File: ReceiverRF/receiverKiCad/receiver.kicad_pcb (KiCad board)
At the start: 2 copper layers, 95 x 60 mm, 75 parts, among them J1 Conn_Coaxial, J2 Conn_01x05_Socket, J3 Conn_01x04, Q1 MMBT3904, SW1 SW_Push, SW2 SW_Push, SW3 SW_Push, SW4 SW_Push, SW5 SW_Nidec_CAS-120A1, U1 STM32F103RET6, U2 NCV5501DT33RKG, U3 NJM2882F05-TE1, U4 MLX90393SLW-ABA-011-RE, Y1 Crystal_GND24

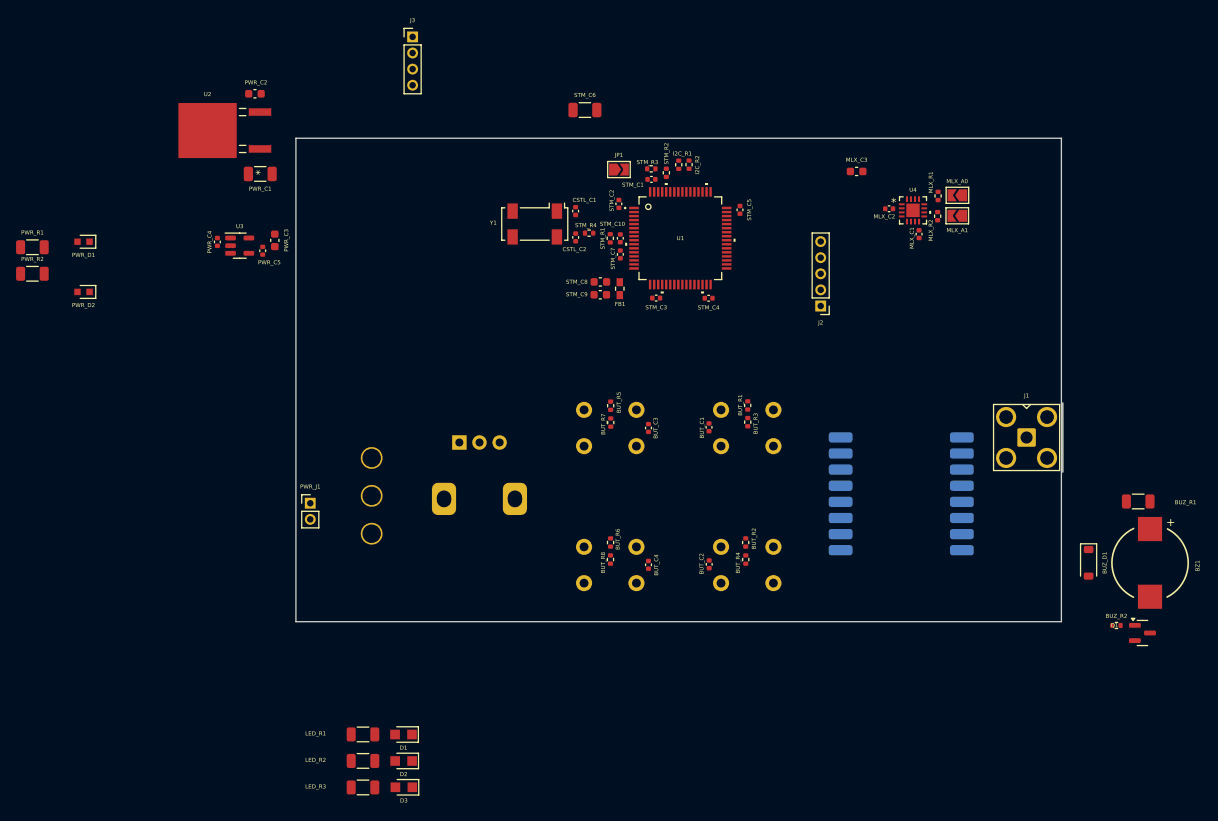
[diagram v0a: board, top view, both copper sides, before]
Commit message: suggestions de Luca et placement sur PCB
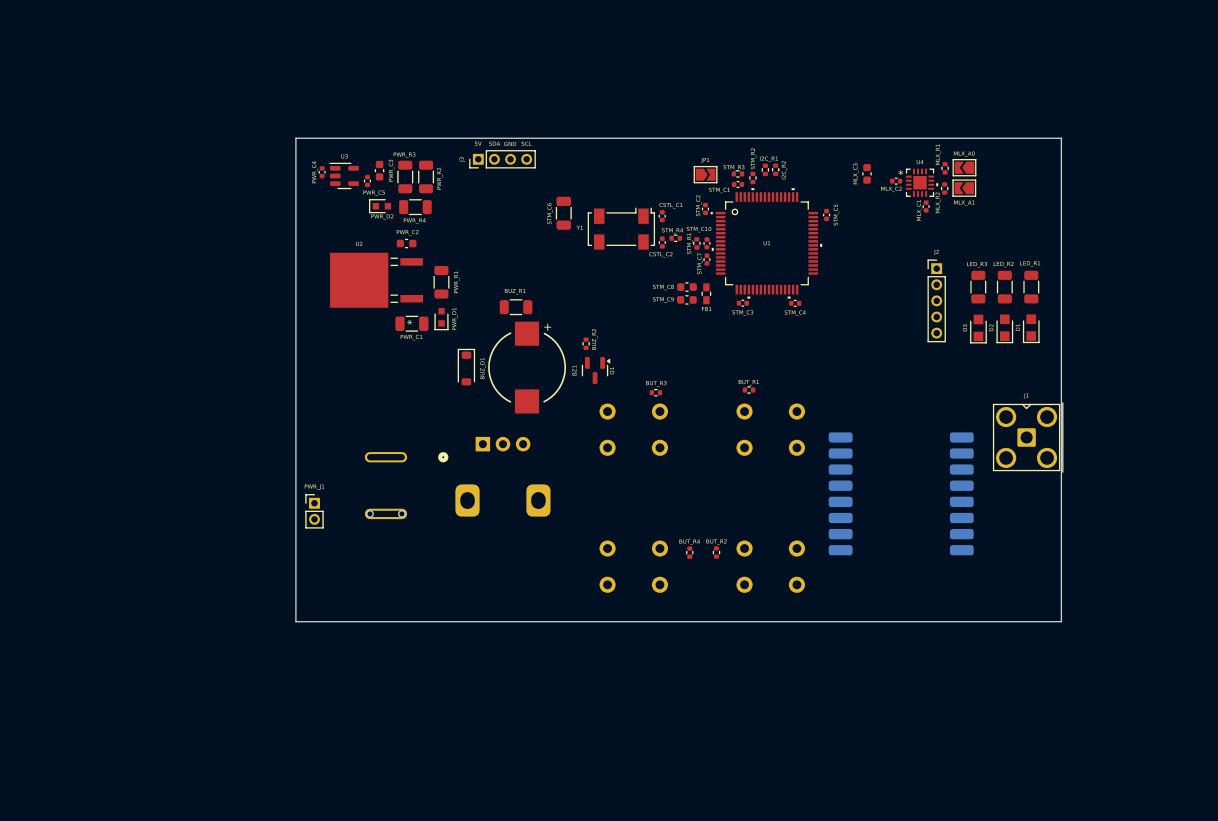
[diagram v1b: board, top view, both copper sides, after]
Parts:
- removed BUT_C1, BUT_C2, BUT_C3, BUT_C4: C, Capacitor_SMD:C_0402_1005Metric
- removed BUT_R5, BUT_R6: 2k, Resistor_SMD:R_0402_1005Metric
- removed BUT_R7, BUT_R8: 10k, Resistor_SMD:R_0402_1005Metric
- added PWR_R3: 145, Resistor_SMD:R_1206_3216Metric, F.Cu at (116.0, 84.5)
- added PWR_R4: 145, Resistor_SMD:R_1206_3216Metric, F.Cu at (114.7, 88.2)
- BUT_R1, BUT_R2: value 2k -> 10k
- PWR_R2: value 330 -> 145
- SW5: value SW_Nidec_CAS-120A1 -> SW_SPST; footprint Footprints:Toggle_SW -> Footprints:D102J12S215PQA_CNK
- moved LED_R1 99.8 mm to (191.1, 98.2), turned to -90 degrees
- moved LED_R2 99.0 mm to (187.8, 98.2), turned to -90 degrees
- moved LED_R3 98.4 mm to (184.5, 98.2), turned to -90 degrees
- moved D1 92.8 mm to (191.1, 103.2), turned to 90 degrees
- moved D2 92.0 mm to (187.8, 103.2), turned to 90 degrees
- moved D3 91.3 mm to (184.5, 103.2), turned to 90 degrees
- moved BZ1 81.0 mm to (128.5, 108.2)
- moved BUZ_D1 80.9 mm to (121.0, 108.3)
- moved BUZ_R1 80.9 mm to (127.1, 100.7)
- moved Q1 75.3 mm to (136.9, 108.5), turned to -90 degrees
- moved BUZ_R2 74.5 mm to (135.8, 105.2), turned to -90 degrees
- moved PWR_R1 51.0 mm to (117.9, 97.6), turned to -90 degrees
- moved PWR_R2 47.8 mm to (113.4, 84.5), turned to -90 degrees
- moved PWR_D1 45.4 mm to (117.9, 101.9), turned to 90 degrees
- moved PWR_D2 38.5 mm to (110.5, 88.1), turned to 0 degrees
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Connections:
- BUT_R1 pad 2: Net-(BUT_R1-Pad2) -> PUSH_1
- BUT_R2 pad 2: Net-(BUT_R2-Pad2) -> PUSH_2
- BUT_R3 pad 1: Net-(BUT_R1-Pad2) -> +3.3V
- BUT_R3 pad 2: PUSH_1 -> PUSH_3
- BUT_R4 pad 1: Net-(BUT_R2-Pad2) -> +3.3V
- BUT_R4 pad 2: PUSH_2 -> PUSH_4
- J3 pad 1: GND -> +5V
- J3 pad 2: +5V -> I2C_SDA
- J3 pad 3: I2C_SDA -> GND
- PWR_R2 pad 2: Net-(PWR_D2-A) -> Net-(PWR_R2-Pad2)
- SW1 pad 1: Net-(BUT_R1-Pad2) -> PUSH_1
- SW2 pad 1: Net-(BUT_R2-Pad2) -> PUSH_2
- SW3 pad 1: Net-(BUT_R5-Pad2) -> PUSH_3
- SW4 pad 1: Net-(BUT_R6-Pad2) -> PUSH_4
- SW5 pad 1: VCC -> Net-(PWR_J1-Pin_1)
- SW5 pad 2: Net-(PWR_J1-Pin_1) -> VCC
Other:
- board text added: "5V"
- board text added: "GND"
- board text added: "SCL"
- board text added: "SDA"

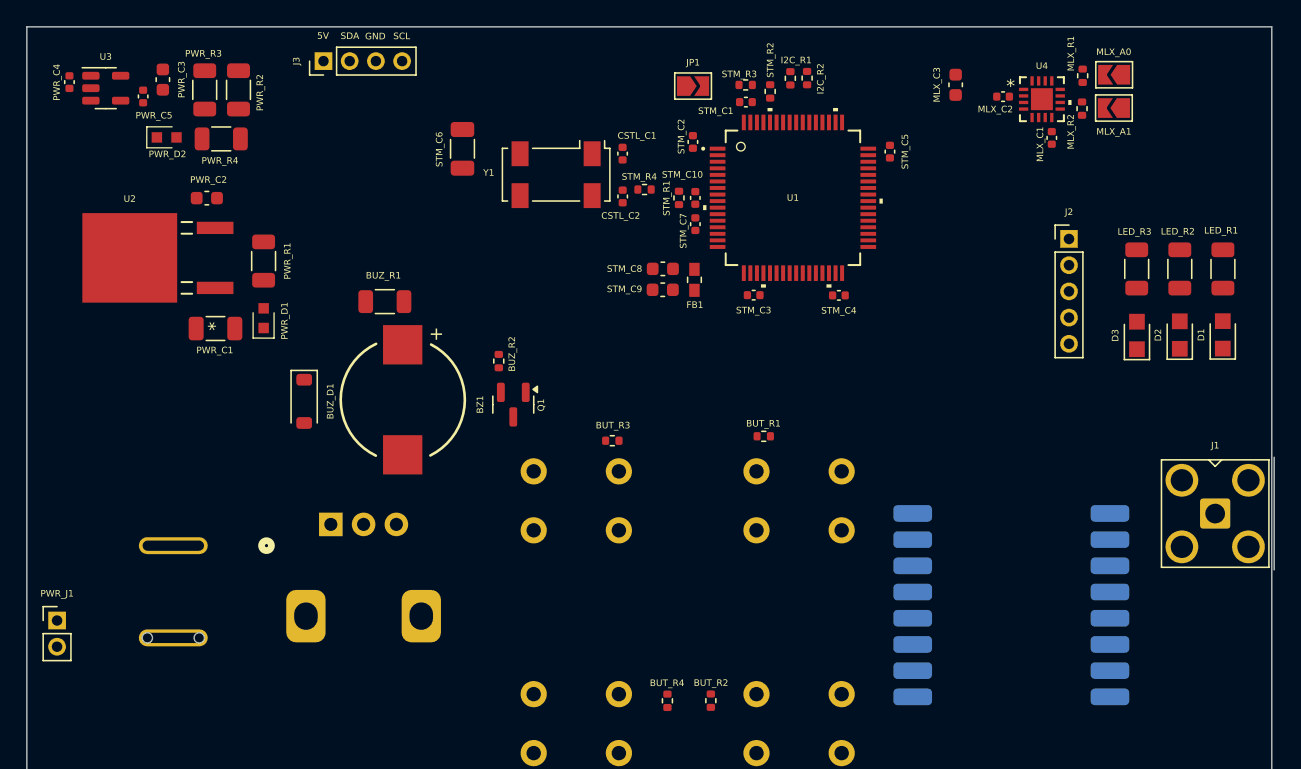
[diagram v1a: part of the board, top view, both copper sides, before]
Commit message: setting du DRC  et layout du silkscreen
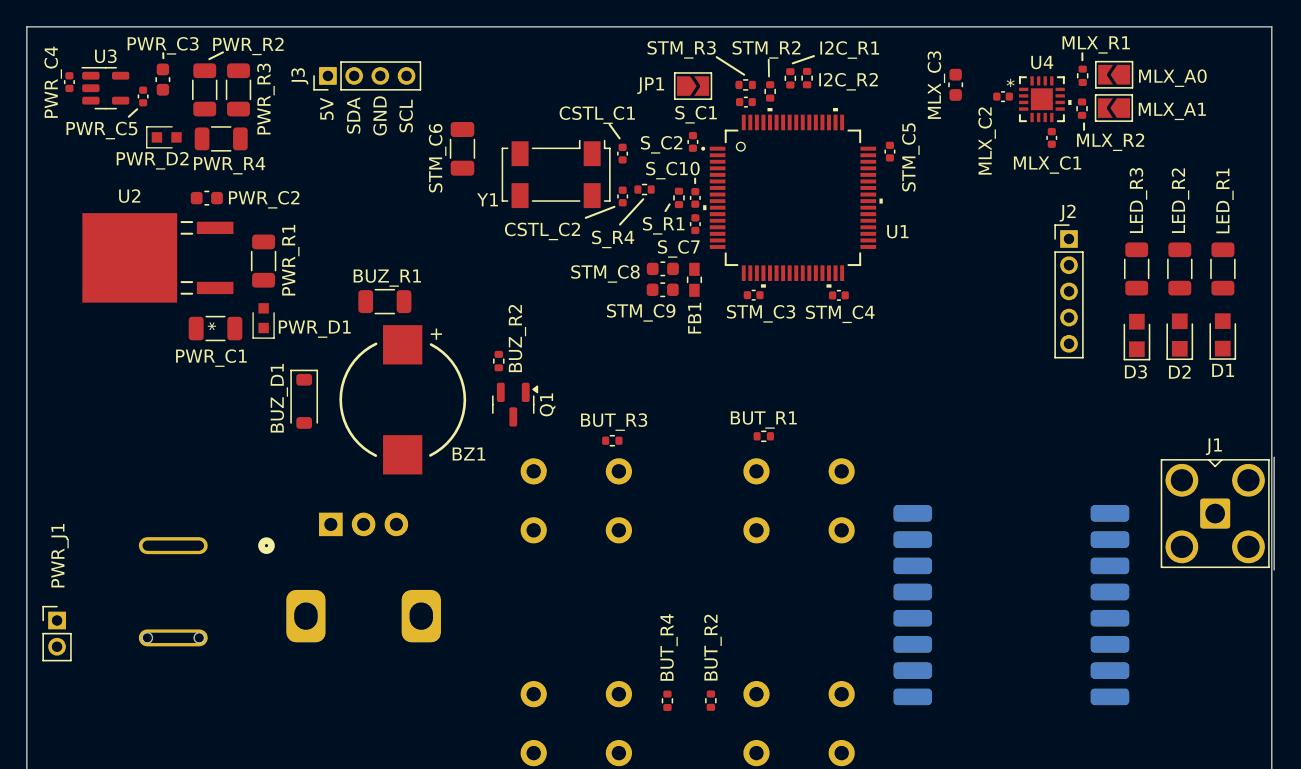
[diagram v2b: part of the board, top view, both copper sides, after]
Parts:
- moved J3 1.18 mm to (122.8, 83.4)
- renumbered STM_C1 to S_C1, STM_C10 to S_C10, STM_C2 to S_C2, STM_C7 to S_C7, STM_R1 to S_R1, STM_R4 to S_R4
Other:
- rule pad_to_mask_clearance: 0 -> 0.038

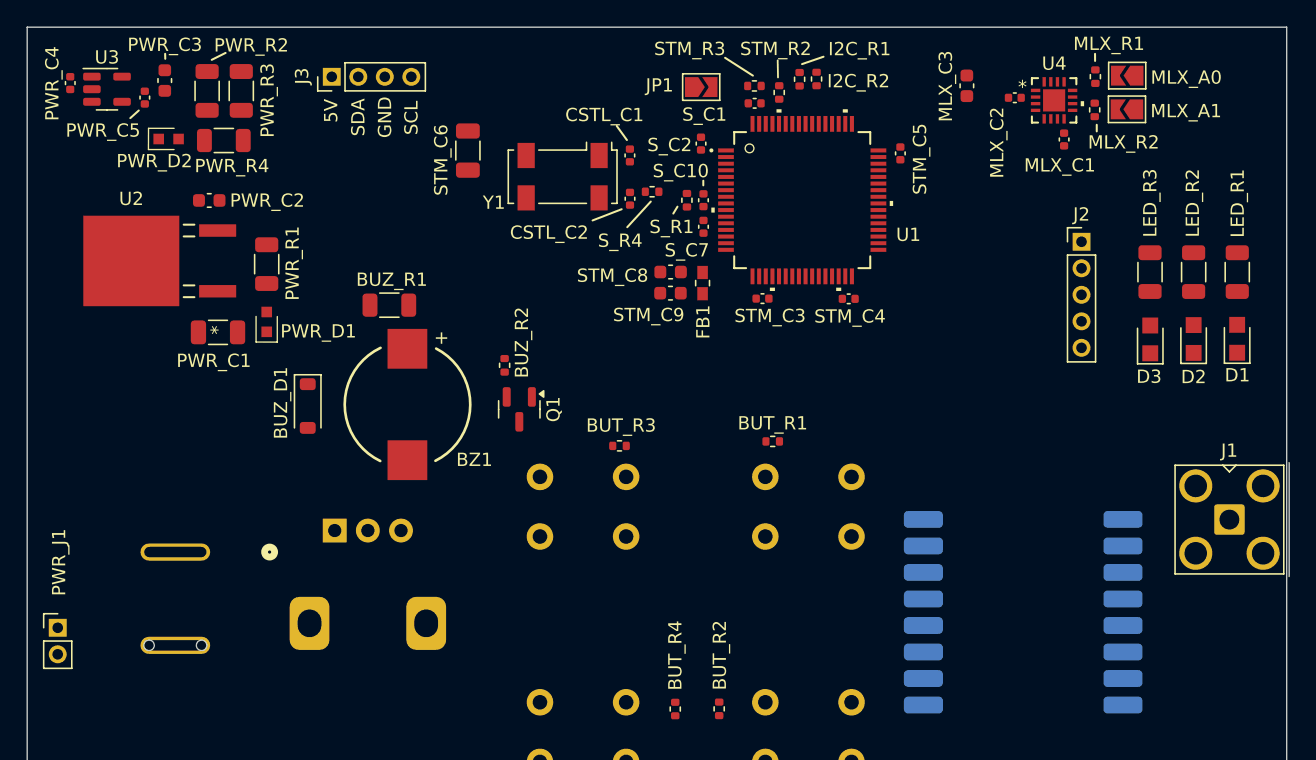
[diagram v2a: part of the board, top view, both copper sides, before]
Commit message: Tracage des groupes et début connexion STM/RFM
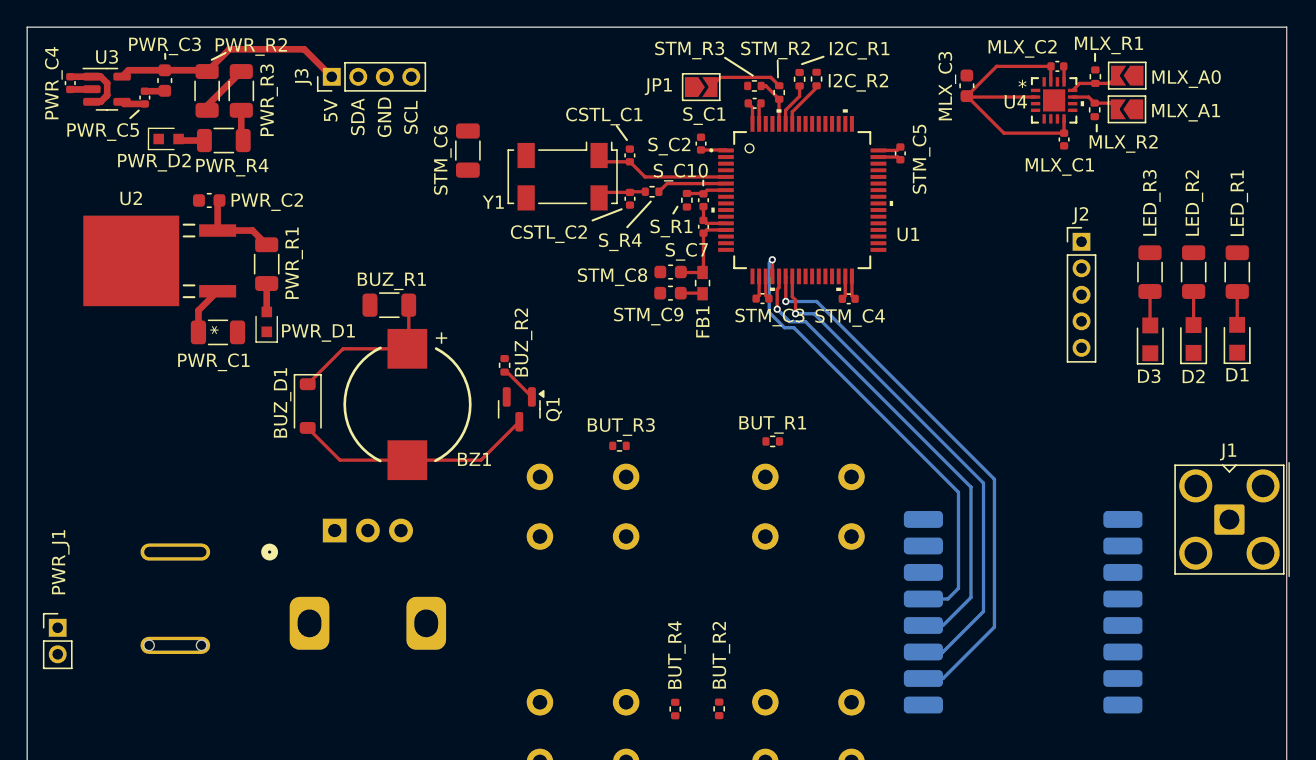
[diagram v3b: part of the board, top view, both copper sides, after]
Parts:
- moved MLX_C2 3.99 mm to (177.5, 82.7), turned to 0 degrees
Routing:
- net SPI_MISO: track 0.00 -> 41.3 mm, vias 0 -> 1
- net +3.3V: track 0.00 -> 40.3 mm
- net SPI_MOSI: track 0.00 -> 37.9 mm, vias 0 -> 1
- net SPI_SCK: track 0.00 -> 35.5 mm, vias 0 -> 1
- net SPI_RFM_CS: track 0.00 -> 35.4 mm, vias 0 -> 1
- net Net-(BUZ_D1-A): track 0.00 -> 18.2 mm
- net +5V: track 0.00 -> 17.6 mm
- net GND: track 0.00 -> 14.1 mm
- net Net-(BUZ_D1-K): track 0.00 -> 12.0 mm
- net OSC_IN: track 0.00 -> 10.2 mm
- net VCC: track 0.00 -> 8.97 mm
- net +3.3VA: track 0.00 -> 6.45 mm
- net Net-(JP1-B): track 0.00 -> 5.72 mm
- net OSC_OUT: track 0.00 -> 5.32 mm
- net Net-(PWR_R2-Pad2): track 0.00 -> 3.99 mm
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
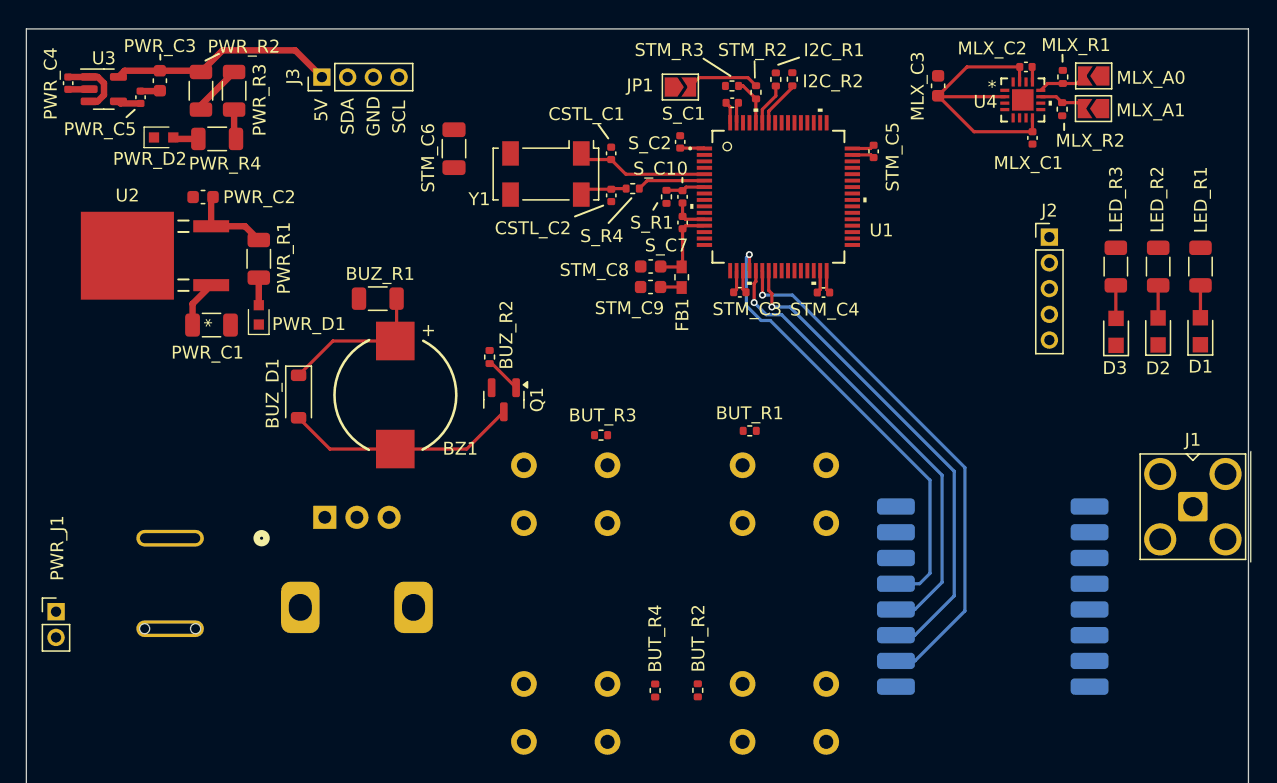
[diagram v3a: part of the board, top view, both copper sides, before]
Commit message: Traçage complet excepté GND et antenne
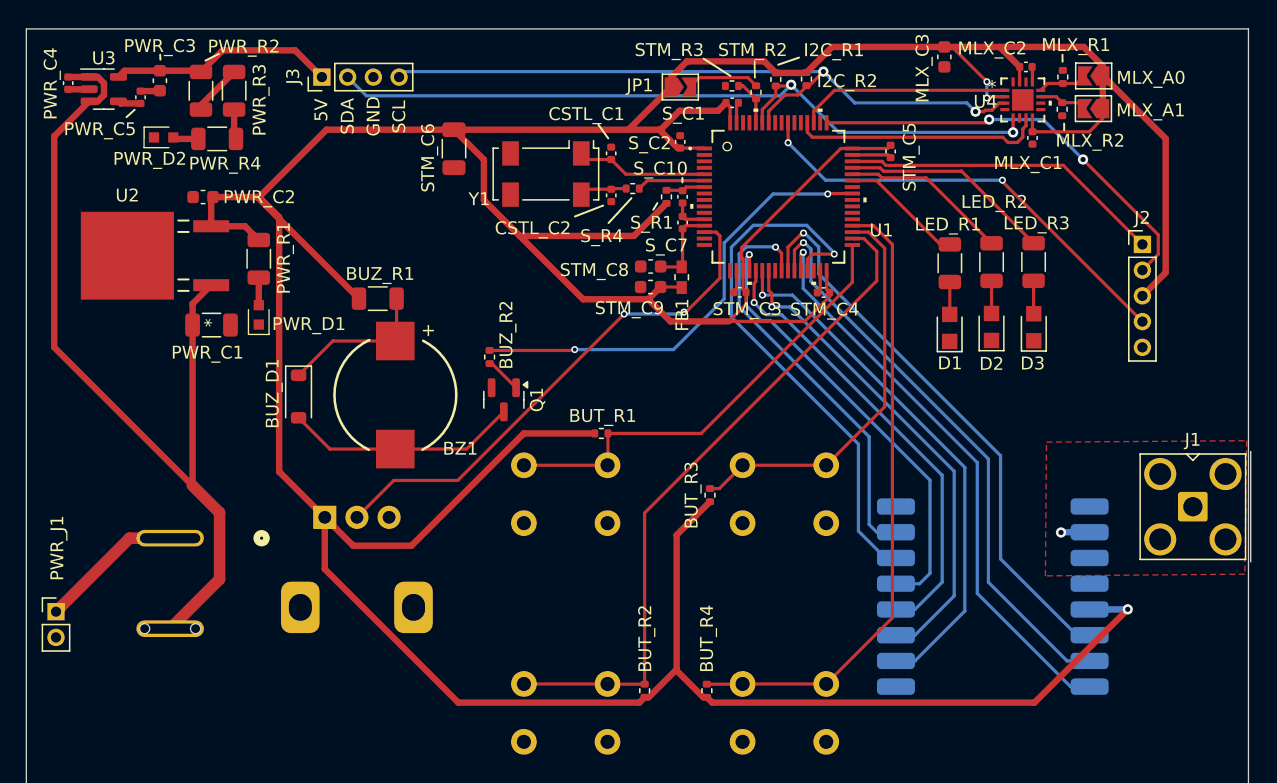
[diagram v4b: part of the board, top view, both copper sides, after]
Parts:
- moved D1 19.5 mm to (171.6, 102.9)
- moved LED_R1 19.5 mm to (171.6, 97.9)
- moved SW1 17.0 mm to (145.0, 113.6)
- moved SW2 17.0 mm to (145.0, 130.6)
- moved SW3 17.0 mm to (162.0, 113.6)
- moved SW4 17.0 mm to (162.0, 130.6)
- moved LED_R2 13.0 mm to (174.9, 97.8)
- moved D2 13.0 mm to (174.8, 102.9)
- moved BUT_R1 11.5 mm to (144.5, 111.1), turned to 0 degrees
- moved BUT_R3 9.67 mm to (153.0, 115.9), turned to 90 degrees
- moved J2 7.25 mm to (186.6, 96.5)
- moved D3 6.40 mm to (178.1, 102.9)
- moved LED_R3 6.40 mm to (178.1, 97.8)
- moved BUT_R2 4.13 mm to (147.9, 131.1)
- moved BUT_R4 4.02 mm to (152.7, 131.1)
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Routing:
- net +3.3V: track 40.3 -> 371.6 mm, vias 0 -> 3
- net VCC: track 8.97 -> 70.5 mm
- net I2C_SDA: track 3.29 -> 59.9 mm, vias 0 -> 2
- net PUSH_2: track 0.00 -> 52.8 mm
- net I2C_SCL: track 3.63 -> 55.3 mm, vias 0 -> 2
- net PUSH_4: track 0.00 -> 49.3 mm
- net RFM_GPIO3: track 0.00 -> 45.4 mm, vias 0 -> 1
- net RFM_GPIO2: track 0.00 -> 45.3 mm, vias 0 -> 1
- net RFM_GPIO1: track 0.00 -> 44.6 mm, vias 0 -> 1
- net RFM_NIRQ: track 0.00 -> 42.8 mm, vias 0 -> 1
- net VOLUME: track 0.00 -> 40.6 mm, vias 0 -> 2
- net BUZZER: track 0.00 -> 35.8 mm, vias 0 -> 2
- net PUSH_1: track 0.00 -> 35.8 mm
- net SYS_TRACESWO: track 0.00 -> 34.9 mm, vias 0 -> 2
- net SYS_SWCLK: track 0.00 -> 32.9 mm, vias 0 -> 2
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- added copper zone on F.Cu, net GND

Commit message: fin traçage et fix erreurs DRC
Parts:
- renumbered S_C1 to STM_C1
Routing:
- net GND: track 17.6 -> 68.1 mm, vias 1 -> 61
- net /Capteurs/ANT: track 0.00 -> 8.04 mm
- net SPI_RFM_CS: track 35.4 -> 37.4 mm
- net RFM_NIRQ: track 42.8 -> 44.4 mm
- net +3.3V: track 371.6 -> 373.2 mm
- net RFM_GPIO1: track 44.6 -> 46.0 mm
- net I2C_SCL: track 55.3 -> 56.4 mm
- net RFM_SDN: track 32.6 -> 33.7 mm
- net RFM_GPIO2: track 45.3 -> 46.2 mm
- net I2C_SDA: track 59.9 -> 60.7 mm
- net SPI_MOSI: track 37.9 -> 37.4 mm
- added copper zone on B.Cu, net GND
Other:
- board size 95 x 60 mm -> 95.4 x 60 mm
